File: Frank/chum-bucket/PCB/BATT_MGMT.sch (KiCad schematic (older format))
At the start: 63 parts

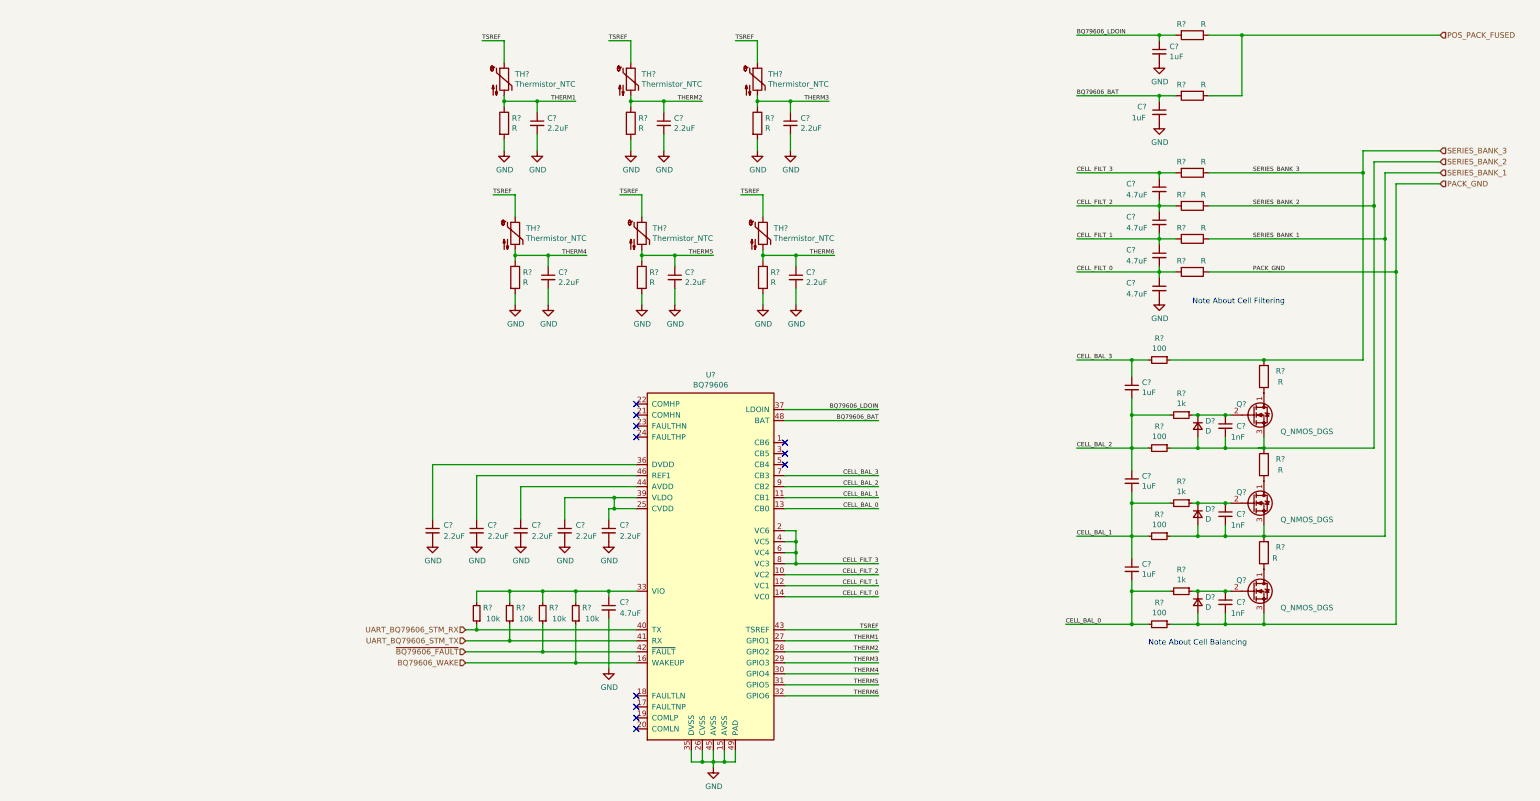
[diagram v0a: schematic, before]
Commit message: minor schematic update + inrush sim
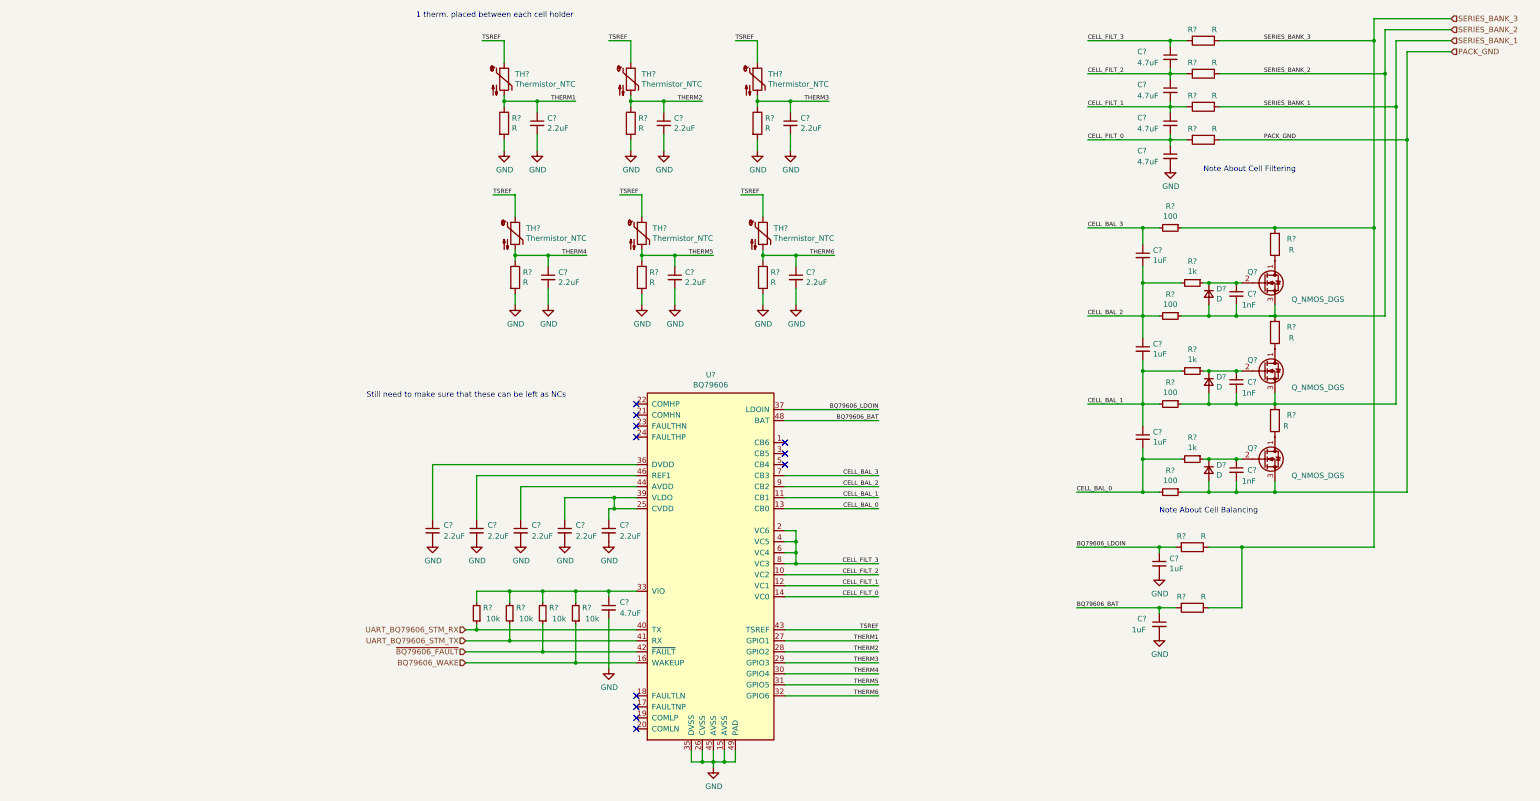
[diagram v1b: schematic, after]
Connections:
- net POS_PACK_FUSED is gone; now on net SERIES_BANK_3: R?.1, R?.1
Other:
- note added: "1 therm. placed between each cell holder"
- note added: "Still need to make sure that these can be left as NCs"
- moved on the sheet: C?, D?, Q?, R?

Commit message: Weekends work. Final component selection then ready for review :)
huge oof
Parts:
- added F?: Fuse, symbol Device:Fuse
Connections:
- net SERIES_BANK_3: now also F?.1; no longer R?.1, R?.1
- new net: F?.2, R?.1, R?.1
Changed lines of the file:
@@
 $Descr A4 11693 8268
 encoding utf-8
-Sheet 5 5
+Sheet 3 6
 Title ""
 Date ""
@@
 Wire Wire Line
 	9800 2550 9800 5450
-Wire Wire Line
-	9800 5450 8600 5450
 Connection ~ 9800 2550
-Connection ~ 8600 5450
 Text Notes 650  4100 0    50   ~ 0
 Still need to make sure that these can be left as NCs
 Text Notes 1100 650  0    50   ~ 0
 1 therm. placed between each cell holder
+$Comp
+L Device:Fuse F?
+U 1 1 5F28DD63
+P 9150 5450
+F 0 "F?" V 8953 5450 50  0000 C CNN
+F 1 "Fuse" V 9044 5450 50  0000 C CNN
+F 2 "" V 9080 5450 50  0001 C CNN
+F 3 "~" H 9150 5450 50  0001 C CNN
+	1    9150 5450
+	0    1    1    0
+$EndComp
+Wire Wire Line
+	9300 5450 9800 5450
+Wire Wire Line
+	9000 5450 8600 5450
+Connection ~ 8600 5450
 $EndSCHEMATC

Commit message: batt-management sheet updates
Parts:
- removed C? (x2): 1nF, symbol Device:C_Small
- removed C? (x3): 4.7uF, symbol Device:C_Small
- removed C?: 1uF, symbol Device:C_Small
- removed D? (x2): D, symbol Device:D_Small
- removed Q? (x2): Q_NMOS_DGS, symbol Device:Q_NMOS_DGS
- removed R? (x2): R, symbol Device:R
- added C? (x2): 1nF, symbol Device:C_Small
- added C?: 0.33uF, symbol Device:C_Small
- added C? (x3): 0.47uF, symbol Device:C_Small
- added D? (x2): BAS16, Diode_SMD:D_SOD-323, symbol Device:D_Small
- added Q? (x2): AON2406, symbol Device:Q_NMOS_DGS
- added R? (x5): 4, Resistor_SMD:R_2512_6332Metric, symbol Device:R
- C?: value 4.7uF -> 0.47uF; Voltage (none) -> 16V
- C?: value 1uF -> 0.33uF; Voltage (none) -> 16V
- D?: value D -> BAS16; footprint (none) -> Diode_SMD:D_SOD-323; Digikey (none) -> BAS16HT3GOSTR-ND
- F?: value Fuse -> 100mA
- Q?: value Q_NMOS_DGS -> AON2406; Digikey (none) -> 785-1491-2-ND; Package (none) -> http://www.aosmd.com/res/packaging_information/DFN2x2B_6L_E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
- R?: value R -> 100
- R?: value R -> 40
- R? (x4): value R -> 47
- R?: value R -> 4; footprint (none) -> Resistor_SMD:R_2512_6332Metric; Digikey (none) -> A121248TR-ND; Power (none) -> 4W
- U?: footprint (none) -> Package_QFP:LQFP-48-1EP_7x7mm_P0.5mm_EP3.6x3.6mm_ThermalVias; Digikey (none) -> 296-BQ79606APHPTQ1TR-ND
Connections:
- net BQ79606_BAT: now also C?.1
- net CELL_BAL_3: now also U?.1 (CB6), U?.3 (CB5), U?.5 (CB4)
- net CELL_FILT_0: now also C?.2
- net CELL_FILT_1: now also C?.1, C?.2
- net CELL_FILT_2: now also C?.1, C?.2
- net CELL_FILT_3: now also C?.1
- net GND: now also C?.2
- net PACK_GND: now also Q?.3 (S)
- net SERIES_BANK_1: now also C?.2, D?.2 (A), Q?.3 (S), R?.2, R?.2
- net SERIES_BANK_2: now also C?.2, D?.2 (A), R?.2, R?.2
- net SERIES_BANK_3: now also R?.2
- net at R?.1: now also C?.1, D?.1 (K), Q?.2 (G)
- net at C?.1, D?.1 (K), R?.1: now also Q?.2 (G)
- net at Q?.1 (D), R?.1: now also R?.1
- net at Q?.2 (G), R?.1: now also C?.1, D?.1 (K)
- new net: Q?.1 (D), R?.1, R?.1 (x2)
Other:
- note added: "<--- BMS IC | CELLS ---->"
- note added: "BALANCE RESISTOR NOTES:\n- parallel 2512 resistor placed incase 1A balance current \nis insufficent\n- selected resistor rated for 2.5W power dissipation, \nbalancing will be internmittent though\n\n"
- note added: "BALANCE TRANSISTOR NOTES\n- Series gate resistor to limit current during hotplug\n- Gate capacitor for power loss during transients\n- Gate diode for ESD protection (no high clamping diode)\n- VGS_min is 3.2/2 V = 1.6V\n- VDS_max is 4.2V"
- note added: "NOTE ABOUT CELL FILTERING:\n- R value to be 4 times the balance resistor\n- Corner fequency is 720Hz\n (well below switch freq of buck) \n"
- note added: "To Do: confirm power supply scenario is ok"
- note removed: "Note About Cell Balancing\n"
- note removed: "Note About Cell Filtering\n"
- note removed: "Still need to make sure that these can be left as NCs"
- moved on the sheet: C?, D?, F?, Q?, R?

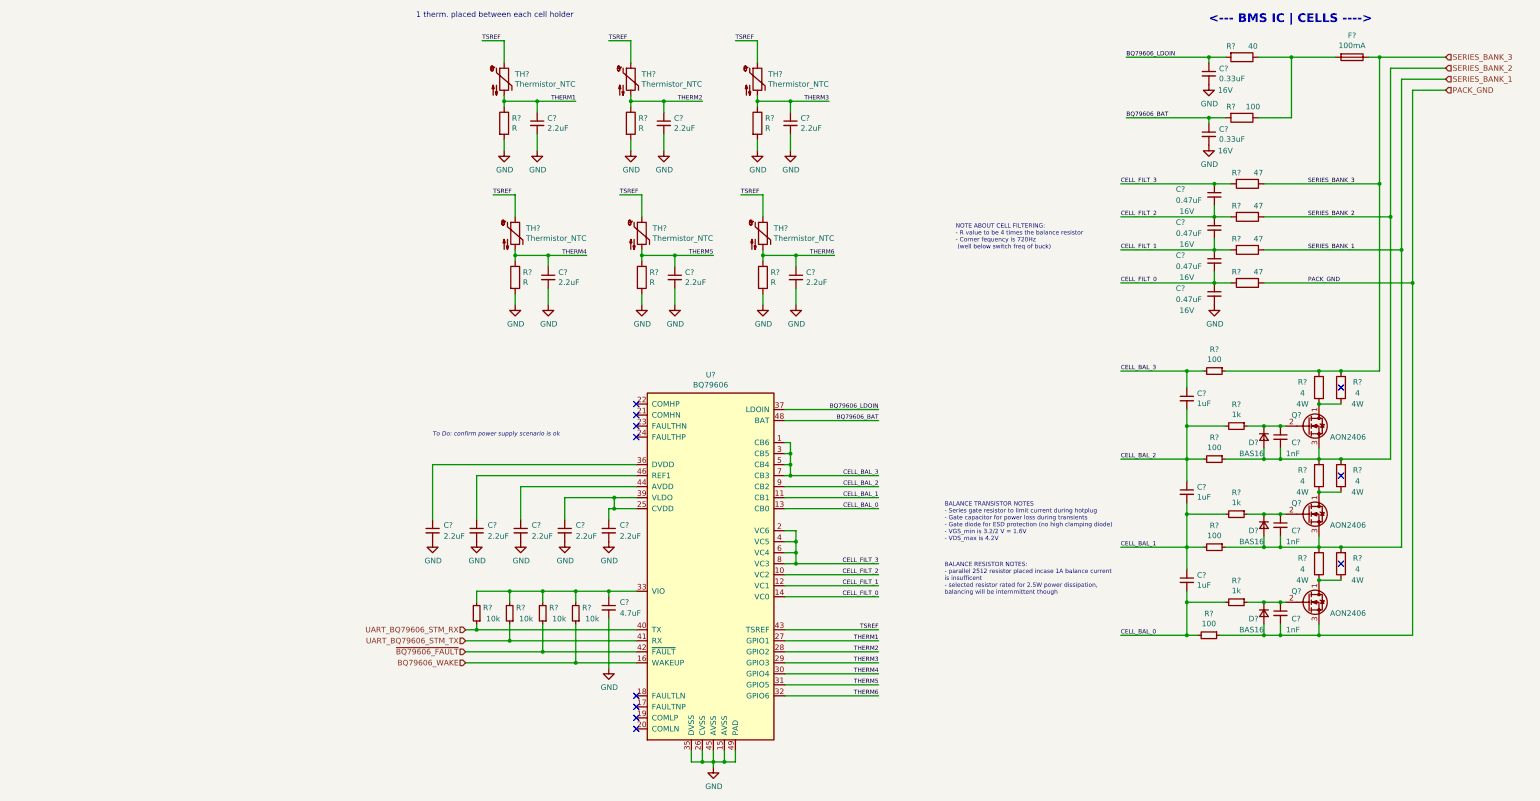
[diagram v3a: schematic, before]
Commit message: Minor schematic organization changes
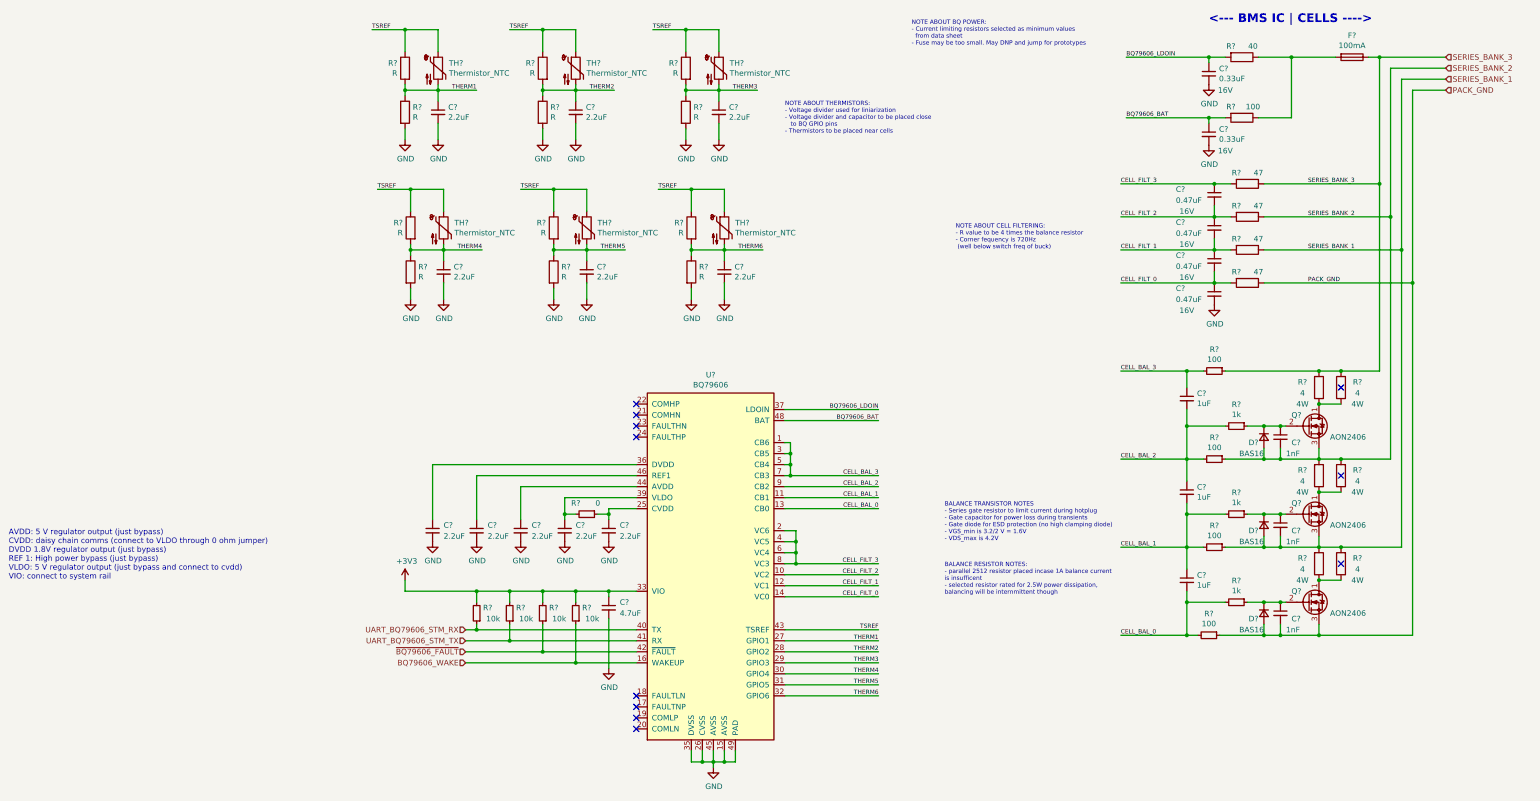
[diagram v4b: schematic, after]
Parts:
- removed C? (x5): 2.2uF, symbol Device:C_Small
- removed R? (x5): R, symbol Device:R
- removed TH? (x5): Thermistor_NTC, symbol Device:Thermistor_NTC
- added C? (x5): 2.2uF, symbol Device:C_Small
- added R? (x11): R, symbol Device:R
- added R?: 0, symbol Device:R_Small
- added TH? (x5): Thermistor_NTC, symbol Device:Thermistor_NTC
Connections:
- net GND: now also C?.2, C?.2, C?.2, C?.2, C?.2, R?.2, R?.2, R?.2, R?.2, R?.2
- net THERM1: now also C?.1, R?.1, R?.2, TH?.2
- net THERM2: now also C?.1, R?.1, R?.2, TH?.2
- net THERM3: now also C?.1, R?.1, R?.2, TH?.2
- net THERM4: now also R?.2
- net THERM5: now also C?.1, R?.1, R?.2, TH?.2
- net THERM6: now also C?.1, R?.1, R?.2, TH?.2
- net TSREF: now also R?.1, R?.1, R?.1, R?.1, R?.1, R?.1, TH?.1, TH?.1, TH?.1, TH?.1, TH?.1
- net +3V3: now reaches C?.1, R?.2, R?.2, R?.2, R?.2, U?.33 (VIO)
- net at C?.1, U?.25 (CVDD): now also R?.1; no longer C?.1, U?.39 (VLDO)
- new net: C?.1, R?.2, U?.39 (VLDO)
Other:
- note added: "AVDD: 5 V regulator output (just bypass) \nCVDD: daisy chain comms (connect to VLDO through 0 ohm jumper) \nDVDD 1.8V regulator output (just bypass) \nREF 1: High power bypass (just bypass) \nVLDO: 5 V regulator output (just bypass and connect to cvdd) \nVIO: connect to system rail"
- note added: "NOTE ABOUT BQ POWER:\n- Current limiting resistors selected as minimum values\n from data sheet\n- Fuse may be too small. May DNP and jump for prototypes\n"
- note added: "NOTE ABOUT THERMISTORS:\n- Voltage divider used for liniarization\n- Voltage divider and capacitor to be placed close\n to BQ GPIO pins\n- Thermistors to be placed near cells"
- note removed: "1 therm. placed between each cell holder"
- note removed: "To Do: confirm power supply scenario is ok"
- moved on the sheet: C?, R?, TH?

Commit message: more work
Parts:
- gave numbers to parts that had none: 74
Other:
- note added: "NOTE ABOUT CELL FILTERING:\n- R value to be 4 times the balance resistor\n- 3db is 720Hz\n (well below switch freq of buck) \n"
- note removed: "NOTE ABOUT CELL FILTERING:\n- R value to be 4 times the balance resistor\n- Corner fequency is 720Hz\n (well below switch freq of buck) \n"
- moved on the sheet: C318, C319, C320, C321, R327, R328, R329, R330

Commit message: changes
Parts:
- removed R334, R335, R336: 4, Resistor_SMD:R_2512_6332Metric, symbol Device:R
- C301, C305, C306, C309: footprint (none) -> Capacitor_SMD:C_0603_1608Metric; Voltage (none) -> 6V
- C302, C303, C307, C308, C311, C312: value 2.2uF -> 10nF; footprint (none) -> Capacitor_SMD:C_0603_1608Metric
- C304: footprint (none) -> Capacitor_SMD:C_0603_1608Metric; Voltage (none) -> 10V
- C310: footprint (none) -> Capacitor_SMD:C_0805_2012Metric
- C313, C314, C315, C316, C317, C318, C319, C320, C321, C322, C323, C324: footprint (none) -> Capacitor_SMD:C_0603_1608Metric
- F301: value 100mA -> 200mA; footprint (none) -> Fuse:Fuse_0603_1608Metric; Digikey (none) -> P15127TR-ND
- R301, R302, R303, R304, R305, R306, R307, R308, R309, R310, R311, R312, R313, R314, R315, R316, R317, R318, R319, R320, R321, R322, R323, R324, R325, R326, R327, R328, R329, R330: footprint (none) -> Resistor_SMD:R_0603_1608Metric
- TH301, TH302, TH303, TH304, TH305, TH306: value Thermistor_NTC -> NTC_TERM; footprint (none) -> Resistor_SMD:R_0603_1608Metric; Digikey (none) -> P12014TR-ND
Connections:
- no-connect marks 11 -> 8
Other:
- note added: "BALANCE RESISTOR NOTES:\n- selected resistor rated for 2.5W power dissipation, \nbalancing will be internmittent though\n\n"
- note removed: "BALANCE RESISTOR NOTES:\n- parallel 2512 resistor placed incase 1A balance current \nis insufficent\n- selected resistor rated for 2.5W power dissipation, \nbalancing will be internmittent though\n\n"

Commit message: ready for review? maybe. (not really)
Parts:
- Q301, Q302, Q303: footprint (none) -> CHUM_BUCKET_FOOTPRINTS:AON2406
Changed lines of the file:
@@
 F 0 "Q301" H 8950 4450 50  0000 L CNN
 F 1 "AON2406" H 9400 4250 50  0000 L CNN
-F 2 "" H 9400 4450 50  0001 C CNN
+F 2 "CHUM_BUCKET_FOOTPRINTS:AON2406" H 9400 4450 50  0001 C CNN
 F 3 "http://www.aosmd.com/res/data_sheets/AON2406.pdf" H 9200 4350 50  0001 C CNN
 F 4 "785-1491-2-ND" H 9200 4350 50  0001 C CNN "Digikey"
@@
 F 0 "Q302" H 8950 5250 50  0000 L CNN
 F 1 "AON2406" H 9400 5050 50  0000 L CNN
-F 2 "" H 9400 5250 50  0001 C CNN
+F 2 "CHUM_BUCKET_FOOTPRINTS:AON2406" H 9400 5250 50  0001 C CNN
 F 3 "http://www.aosmd.com/res/data_sheets/AON2406.pdf" H 9200 5150 50  0001 C CNN
 F 4 "785-1491-2-ND" H 9200 5150 50  0001 C CNN "Digikey"
@@
 F 0 "Q303" H 8950 6050 50  0000 L CNN
 F 1 "AON2406" H 9400 5850 50  0000 L CNN
-F 2 "" H 9400 6050 50  0001 C CNN
+F 2 "CHUM_BUCKET_FOOTPRINTS:AON2406" H 9400 6050 50  0001 C CNN
 F 3 "http://www.aosmd.com/res/data_sheets/AON2406.pdf" H 9200 5950 50  0001 C CNN
 F 4 "785-1491-2-ND" H 9200 5950 50  0001 C CNN "Digikey"
